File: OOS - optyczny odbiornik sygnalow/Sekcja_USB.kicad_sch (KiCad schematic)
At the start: 0 parts

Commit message: Add review notes for DCDC_Boost page
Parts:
- added J6: USB_C_Receptacle, Connector_USB:USB_C_Receptacle_Amphenol_12401548E4-2A, symbol Connector:USB_C_Receptacle
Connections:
- new net: J6.A1 (GND), J6.A12 (GND), J6.B1 (GND), J6.B12 (GND)
- new net: J6.A4 (VBUS), J6.A9 (VBUS), J6.B4 (VBUS), J6.B9 (VBUS)
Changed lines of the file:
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@@
+		)
+	)
+	(text_box "Layout note:\n"
+		(exclude_from_sim no)
+		(at 40.64 150.495 0)
+		(size 25.4 46.355)
+		(margins 0.9525 0.9525 0.9525 0.9525)
+		(stroke
+			(width 0.2032)
+			(type solid)
+			(color 0 0 0 1)
+		)
+		(fill
+			(type color)
+			(color 115 174 255 1)
+		)
+		(effects
+			(font
+				(size 1.27 1.27)
+				(thickness 0.254)
+				(bold yes)
+			)
+			(justify left top)
+		)
+	)
+	(text_box "Project note:"
+		(exclude_from_sim no)
+		(at 12.7 150.495 0)
+		(size 25.4 46.355)
+		(margins 0.9525 0.9525 0.9525 0.9525)
+		(stroke
+			(width 0.2032)
+			(type solid)
+			(color 0 0 0 1)
+		)
+		(fill
+			(type color)
+			(color 255 148 36 1)
+		)
+		(effects
+			(font
+				(size 1.27 1.27)
+				(thickness 0.254)
+				(bold yes)
+			)
+			(justify left top)
+		)
+	)
+	(text_box "Design note:"
+		(exclude_from_sim no)
+		(at 68.58 150.495 0)
+		(size 25.4 46.355)
+		(margins 0.9525 0.9525 0.9525 0.9525)
+		(stroke
+			(width 0.2032)
+			(type solid)
+			(color 0 0 0 1)
+		)
+		(fill
+			(type color)
+			(color 255 231 103 1)
+		)
+		(effects
+			(font
+				(size 1.27 1.27)
+				(thickness 0.254)
+				(bold yes)
+			)
+			(justify left top)
 		)
 	)
@@
 		)
 	)
+	(symbol
+		(lib_id "Connector:USB_C_Receptacle")
+		(at 100.33 83.82 0)
+		(unit 1)
+		(exclude_from_sim no)
+		(in_bom yes)
+		(on_board yes)
+		(dnp no)
+		(fields_autoplaced yes)
+		(property "Reference" "J6"
+			(at 100.33 50.8 0)
+			(effects
+				(font
+					(size 1.27 1.27)
+				)
+			)
+		)
+		(property "Value" "USB_C_Receptacle"
+			(at 100.33 53.34 0)
+			(effects
+				(font
+					(size 1.27 1.27)
+				)
+			)
+		)
+		(property "Footprint" "Connector_USB:USB_C_Receptacle_Amphenol_12401548E4-2A"
+			(at 104.14 83.82 0)
+			(effects
+				(font
+					(size 1.27 1.27)
+				)
+				(hide yes)
+			)
+		)
+		(property "Datasheet" "https://www.usb.org/sites/default/files/documents/usb_type-c.zip"
+			(at 104.14 83.82 0)
+			(effects
+				(font
+					(size 1.27 1.27)
+				)
+				(hide yes)
+			)
+		)
+		(property "Description" "USB Full-Featured Type-C Receptacle connector"
+			(at 100.33 83.82 0)
+			(effects
+				(font
+					(size 1.27 1.27)
+				)
+				(hide yes)
+			)
+		)
+		(pin "A9"
+		)
+		(pin "A4"
+		)
+		(pin "B12"
+		)
+		(pin "B1"
+		)
+		(pin "A12"
+		)
+		(pin "A1"
+		)
+		(pin "S1"
+		)
+		(pin "A10"
+		)
+		(pin "B4"
+		)
+		(pin "B8"
+		)
+		(pin "B2"
+		)
+		(pin "A11"
+		)
+		(pin "B10"
+		)
+		(pin "B9"
+		)
+		(pin "B11"
+		)
+		(pin "A3"
+		)
+		(pin "B5"
+		)
+		(pin "A5"
+		)
+		(pin "B7"
+		)
+		(pin "A6"
+		)
+		(pin "A7"
+		)
+		(pin "A8"
+		)
+		(pin "A2"
+		)
+		(pin "B6"
+		)
+		(pin "B3"
+		)
+		(instances
+			(project ""
+				(path "/635760df-3241-4f53-aa67-bcf04a8ecd85/af862a95-6c6f-4b8d-b6e2-8f113ad068f6"
+					(reference "J6")
+					(unit 1)
+				)
+			)
+		)
+	)

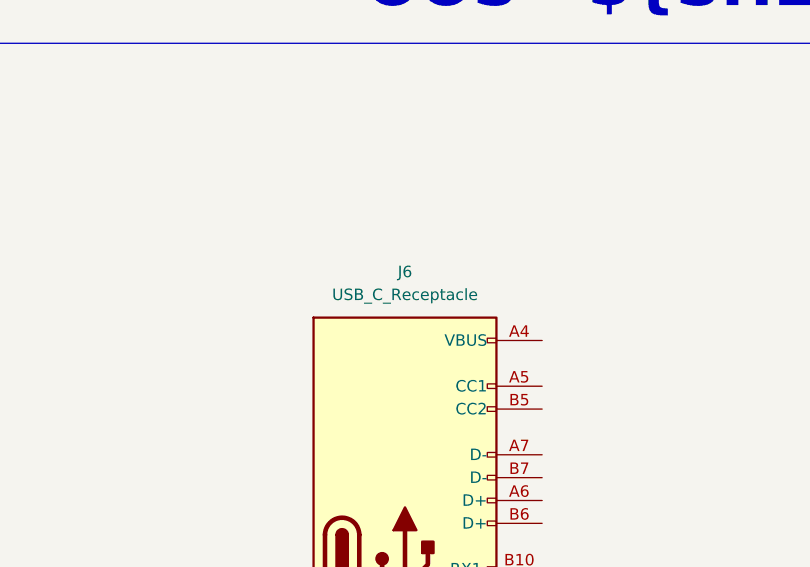
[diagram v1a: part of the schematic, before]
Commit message: Solved points from review on page OOS - Analog
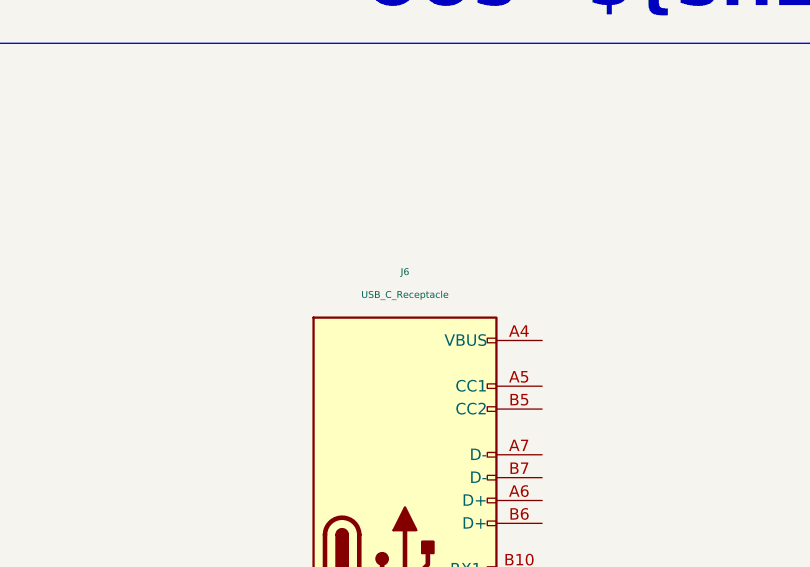
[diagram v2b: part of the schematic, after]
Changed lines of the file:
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@@
 			(effects
 				(font
-					(size 1.27 1.27)
+					(size 0.762 0.762)
 				)
 			)
@@
 			(effects
 				(font
-					(size 1.27 1.27)
+					(size 0.762 0.762)
 				)
 			)
@@
 			(effects
 				(font
-					(size 1.27 1.27)
+					(size 0.762 0.762)
 				)
 				(hide yes)
@@
 			(effects
 				(font
-					(size 1.27 1.27)
+					(size 0.762 0.762)
 				)
 				(hide yes)
@@
 			(effects
 				(font
-					(size 1.27 1.27)
+					(size 0.762 0.762)
 				)
 				(hide yes)
